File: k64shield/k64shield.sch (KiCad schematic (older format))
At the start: 7 parts, among them J1 top_left_header_02x08, J2 bottom_left_header_02x06, J3 rpi_motor_driver_header, J4 top_right_header_02x10, J5 bottom_right_header_02x08, J6 camera_header_01x05, J7 servo_header_01x03

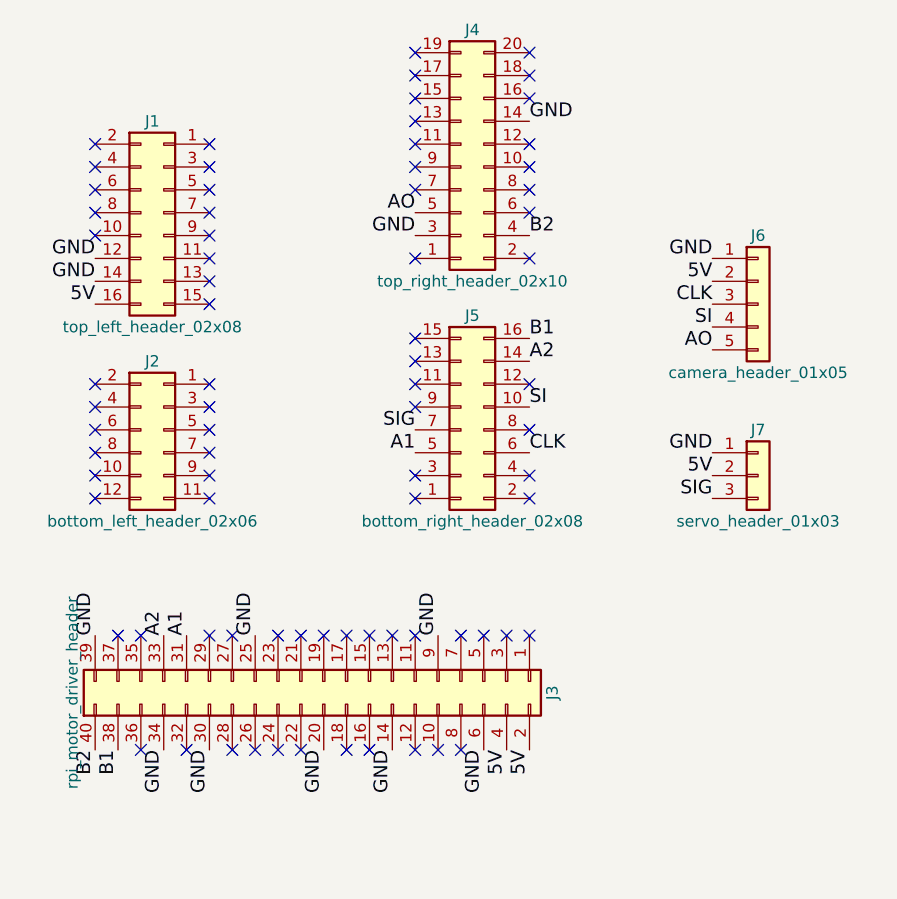
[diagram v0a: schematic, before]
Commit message: Saving so I have a point to revert to - pins are very messed up
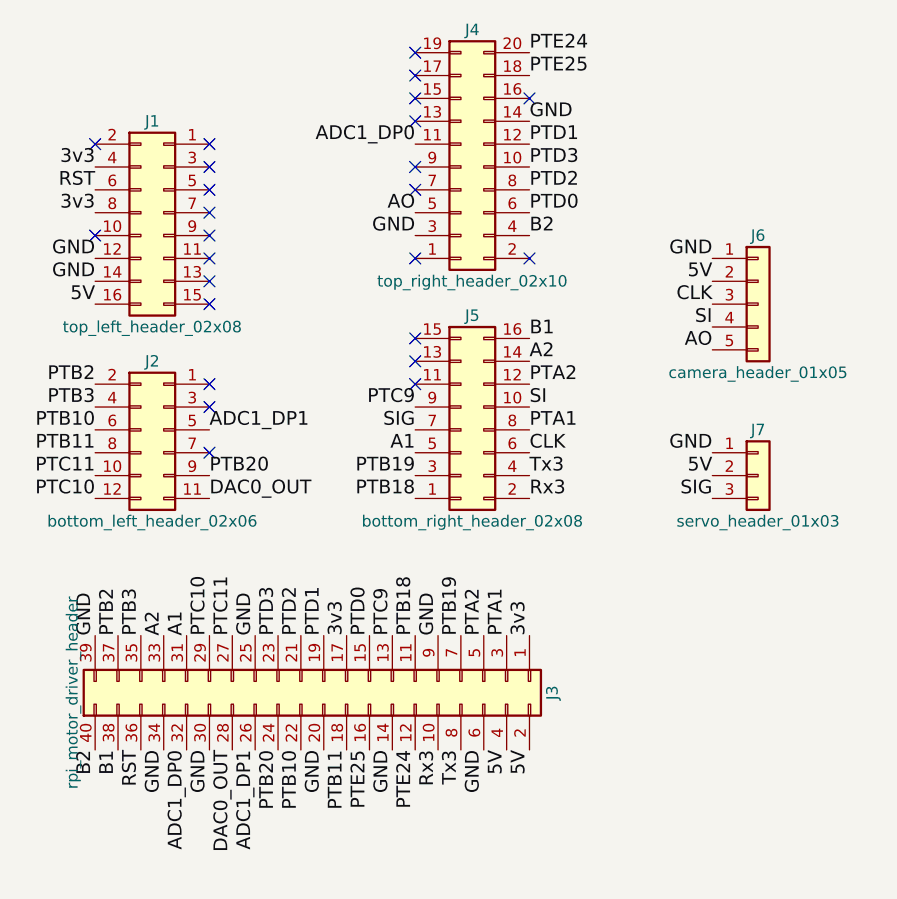
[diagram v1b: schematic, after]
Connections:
- net 3v3: now reaches J1.4 (P3V3-4)
- net 3v3: now also J1.8 (P3V3-8), J3.1 (3v3-1), J3.17 (3v3-17)
- net RST: now reaches J1.6 (RESET-6)
- net RST: now also J3.36 (P27-36)
- net PTC11: now reaches J2.10 (PTC11-10)
- net PTC11: now also J3.27 (IDSO-27)
- net DAC0_OUT: now reaches J2.11 (DAC0_OUT-11)
- net DAC0_OUT: now also J3.28 (IDSC-28)
- net PTC10: now reaches J2.12 (PTC10-12)
- net PTC10: now also J3.29 (P21-29)
- net PTB2: now reaches J2.2 (PTB2-2)
- net PTB2: now also J3.37 (P25-37)
- net PTB3: now reaches J2.4 (PTB3-4)
- net PTB3: now also J3.35 (P24-35)
- net ADC1_DP1: now reaches J2.5 (ADC1_DP1-5)
- net ADC1_DP1: now also J3.26 (CE1-26)
- net PTB10: now reaches J2.6 (PTB10-6)
- net PTB10: now also J3.22 (P6-22)
- net PTB11: now reaches J2.8 (PTB11-8)
- net PTB11: now also J3.18 (P5-18)
- net PTB20: now reaches J2.9 (PTB20-9)
- net PTB20: now also J3.24 (CE0-24)
- net PTD3: now reaches J4.10 (PTD3-10)
- net PTD3: now also J3.23 (SCK-23)
- net ADC1_DP0: now reaches J4.11 (ADC1_DP0-11)
- net ADC1_DP0: now also J3.32 (P26-32)
- net PTD1: now reaches J4.12 (PTD1-12)
- net PTD1: now also J3.19 (MOSI-19)
- net PTE25: now reaches J4.18 (PTE25-18)
- net PTE25: now also J3.16 (P4-16)
- net PTE24: now reaches J4.20 (PTE24-20)
- net PTE24: now also J3.12 (P1-12)
- net PTD0: now reaches J4.6 (PTD0-6)
- net PTD0: now also J3.15 (P3-15)
- net PTD2: now reaches J4.8 (PTD2-8)
- net PTD2: now also J3.21 (MISO-21)
- net PTB18: now reaches J5.1 (PTB18-1)
- net PTB18: now also J3.11 (P0-11)
- net PTA2: now reaches J5.12 (PTA2-12)
- net PTA2: now also J3.5 (SCL-5)
- net Rx3: now reaches J5.2 (PTC16-2)
- net Rx3: now also J3.10 (RX-10)
- net PTB19: now reaches J5.3 (PTB19-3)
- net PTB19: now also J3.7 (P7-7)
- net Tx3: now reaches J5.4 (PTC17-4)
- net Tx3: now also J3.8 (TX-8)
- net PTA1: now reaches J5.8 (PTA1-8)
- net PTA1: now also J3.3 (SDA-3)
- net PTC9: now reaches J5.9 (PTC9-9)
- net PTC9: now also J3.13 (P2-13)
- no-connect marks 77 -> 25
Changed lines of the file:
@@
 SIG
 NoConn ~ 5900 2550
-NoConn ~ 5900 2650
-NoConn ~ 5900 2750
-NoConn ~ 5900 2850
 NoConn ~ 5900 2950
 NoConn ~ 6400 2550
@@
 NoConn ~ 6400 3150
 NoConn ~ 6400 3250
-NoConn ~ 5900 3600
-NoConn ~ 5900 3700
-NoConn ~ 5900 3800
-NoConn ~ 5900 3900
-NoConn ~ 5900 4000
-NoConn ~ 5900 4100
-NoConn ~ 6400 4100
-NoConn ~ 6400 4000
 NoConn ~ 6400 3900
-NoConn ~ 6400 3800
 NoConn ~ 6400 3700
 NoConn ~ 6400 3600
@@
 NoConn ~ 7300 2350
 NoConn ~ 7300 2450
-NoConn ~ 7300 2550
 NoConn ~ 7300 2650
 NoConn ~ 7300 2750
 NoConn ~ 7300 3050
 NoConn ~ 7800 3050
-NoConn ~ 7800 2850
-NoConn ~ 7800 2750
-NoConn ~ 7800 2650
-NoConn ~ 7800 2550
 NoConn ~ 7800 2350
-NoConn ~ 7800 2250
-NoConn ~ 7800 2150
-NoConn ~ 7800 4100
-NoConn ~ 7800 4000
-NoConn ~ 7800 3800
-NoConn ~ 7800 3600
 NoConn ~ 7300 3400
 NoConn ~ 7300 3500
 NoConn ~ 7300 3600
-NoConn ~ 7300 3700
-NoConn ~ 7300 4000
-NoConn ~ 7300 4100
-NoConn ~ 6000 4700
-NoConn ~ 6100 4700
-NoConn ~ 6100 5200
-NoConn ~ 6400 4700
-NoConn ~ 6300 5200
-NoConn ~ 6500 5200
-NoConn ~ 6500 4700
-NoConn ~ 6700 4700
-NoConn ~ 6800 4700
-NoConn ~ 6900 4700
-NoConn ~ 7000 4700
-NoConn ~ 7100 4700
-NoConn ~ 7200 4700
-NoConn ~ 7300 4700
-NoConn ~ 7500 4700
-NoConn ~ 7600 4700
-NoConn ~ 7700 4700
-NoConn ~ 7800 4700
-NoConn ~ 7500 5200
-NoConn ~ 7400 5200
-NoConn ~ 7300 5200
-NoConn ~ 7100 5200
-NoConn ~ 7000 5200
-NoConn ~ 6800 5200
-NoConn ~ 6700 5200
-NoConn ~ 6600 5200
+Text Label 7800 4100 0    60   ~ 0
+Rx3
+Text Label 7400 5200 3    60   ~ 0
+Rx3
+Text Label 7800 4000 0    60   ~ 0
+Tx3
+Text Label 7500 5200 3    60   ~ 0
+Tx3
+Text Label 5900 2650 2    60   ~ 0
+3v3
+Text Label 5900 2850 2    60   ~ 0
+3v3
+Text Label 7800 4700 1    60   ~ 0
+3v3
+Text Label 7000 4700 1    60   ~ 0
+3v3
+Text Label 7800 3800 0    60   ~ 0
+PTA1
+Text Label 7700 4700 1    60   ~ 0
+PTA1
+Text Label 7800 3600 0    60   ~ 0
+PTA2
+Text Label 7600 4700 1    60   ~ 0
+PTA2
+Text Label 5900 3600 2    60   ~ 0
+PTB2
+Text Label 6000 4700 1    60   ~ 0
+PTB2
+Text Label 5900 3700 2    60   ~ 0
+PTB3
+Text Label 6100 4700 1    60   ~ 0
+PTB3
+Text Label 7300 4000 2    60   ~ 0
+PTB19
+Text Label 7500 4700 1    60   ~ 0
+PTB19
+Text Label 7300 4100 2    60   ~ 0
+PTB18
+Text Label 7300 4700 1    60   ~ 0
+PTB18
+Text Label 7300 3700 2    60   ~ 0
+PTC9
+Text Label 7200 4700 1    60   ~ 0
+PTC9
+Text Label 5900 4100 2    60   ~ 0
+PTC10
+Text Label 6400 4700 1    60   ~ 0
+PTC10
+Text Label 5900 4000 2    60   ~ 0
+PTC11
+Text Label 6500 4700 1    60   ~ 0
+PTC11
+Text Label 7800 2850 0    60   ~ 0
+PTD0
+Text Label 7100 4700 1    60   ~ 0
+PTD0
+Text Label 7800 2550 0    60   ~ 0
+PTD1
+Text Label 6900 4700 1    60   ~ 0
+PTD1
+Text Label 7800 2750 0    60   ~ 0
+PTD2
+Text Label 6800 4700 1    60   ~ 0
+PTD2
+Text Label 7800 2650 0    60   ~ 0
+PTD3
+Text Label 6700 4700 1    60   ~ 0
+PTD3
+Text Label 7800 2150 0    60   ~ 0
+PTE24
+Text Label 7300 5200 3    60   ~ 0
+PTE24
+Text Label 7800 2250 0    60   ~ 0
+PTE25
+Text Label 7100 5200 3    60   ~ 0
+PTE25
+Text Label 5900 2750 2    60   ~ 0
+RST
+Text Label 6100 5200 3    60   ~ 0
+RST
+Text Label 7300 2550 2    60   ~ 0
+ADC1_DP0
+Text Label 6300 5200 3    60   ~ 0
+ADC1_DP0
+Text Label 6400 4100 0    60   ~ 0
+DAC0_OUT
+Text Label 6500 5200 3    60   ~ 0
+DAC0_OUT
+Text Label 6400 3800 0    60   ~ 0
+ADC1_DP1
+Text Label 6600 5200 3    60   ~ 0
+ADC1_DP1
+Text Label 6400 4000 0    60   ~ 0
+PTB20
+Text Label 6700 5200 3    60   ~ 0
+PTB20
+Text Label 5900 3800 2    60   ~ 0
+PTB10
+Text Label 6800 5200 3    60   ~ 0
+PTB10
+Text Label 7000 5200 3    60   ~ 0
+PTB11
+Text Label 5900 3900 2    60   ~ 0
+PTB11
 $EndSCHEMATC
